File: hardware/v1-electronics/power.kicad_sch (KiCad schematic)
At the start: 35 parts, among them IC1 TPS61288LRQQR, IC2 MP2721GRH-0000-Z, J1 Female USB-C USB2.0, J2 Female JST-SH, SW7 SW_Push

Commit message: checkpoint(v1 hardware): this is the save before corrections
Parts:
- SW7: value SW_Push -> SW_SPDT; symbol Switch:SW_Push -> Switch:SW_SPDT
- renumbered D86 to D87
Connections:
- net V_IN_TPS: now also SW7.3 (C); no longer SW7.2
- net V_OUT_MP: now also SW7.2 (B); no longer SW7.1
- net VDD renamed V_REG0
- net V_OUT renamed +5V
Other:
- note added: "Consider adding a fuel gauge ic: - i2c and led indictor - BQ27220"
- note added: "is this the simplest power/usb-c module possible? Centralize the decoupling for +5V"
- note removed: "Consider Alternative Chargers: - BQ25883 [2 cell](i2c, power path, boost charger) - BQ25188 (i2c, power path) - BQ25619 Redo your power budget Consider adding a fuel gauge ic: - i2c and led indictor - BQ27220"
- note removed: "Figure out the battery situation and circuitry Conpare BQ25186DLHR and BQ25185DLHR"
- note removed: "Loose Notes"
- note removed: "is this the simplest power/usb-c module possible? Centralize the decoupling for V_SYS"
- moved on the sheet: C45, R56

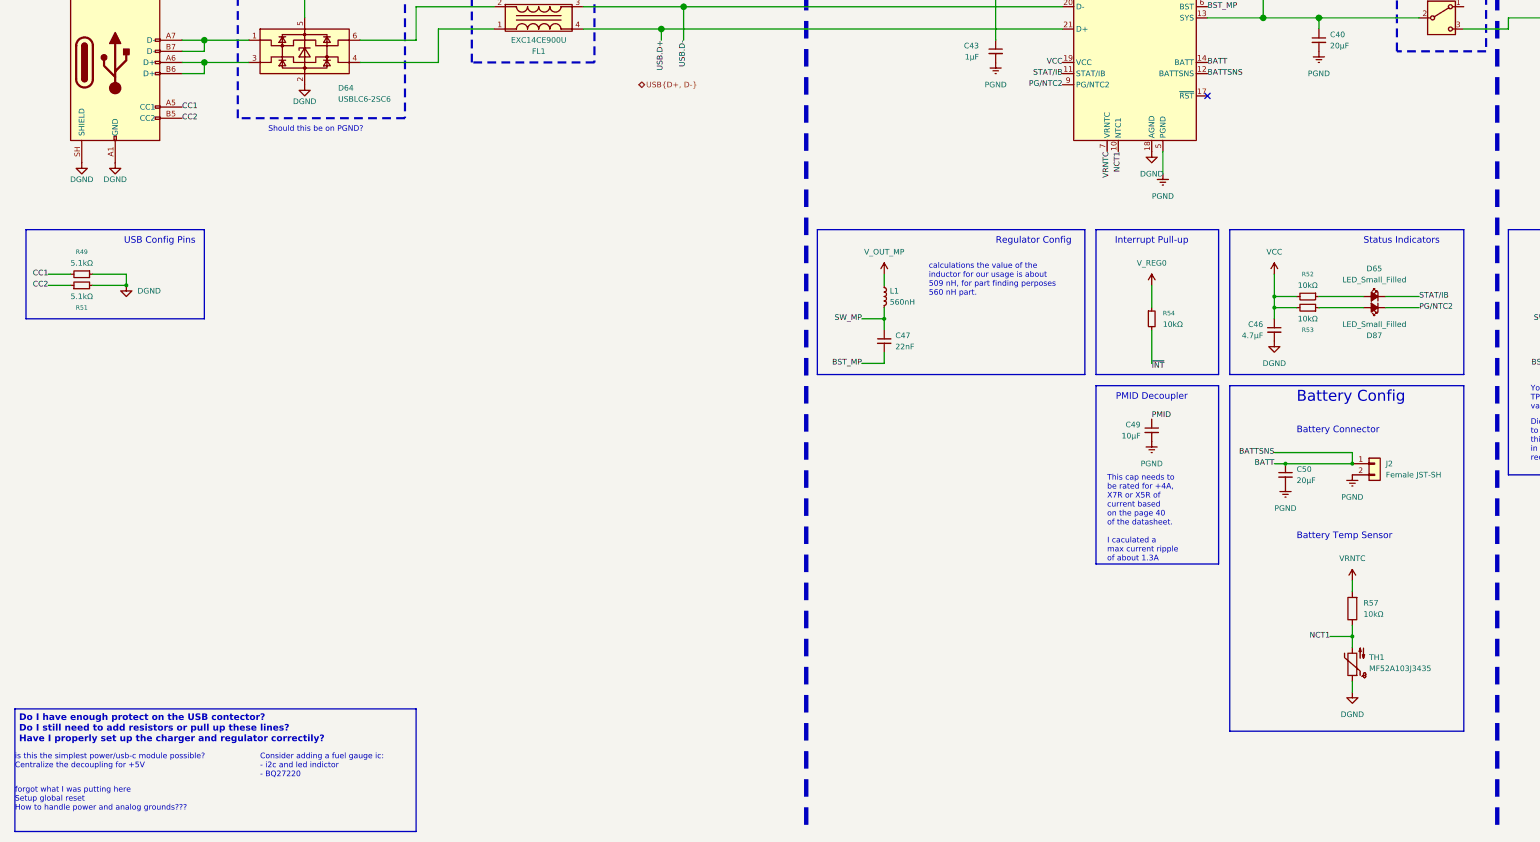
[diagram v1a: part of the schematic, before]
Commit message: fix(v1 hardware): implementing recommendations from Cyril
- rated the lines for the power system
- using a properly rated connecter for the battery
- added manual usb cc detection
- short grounds to each other
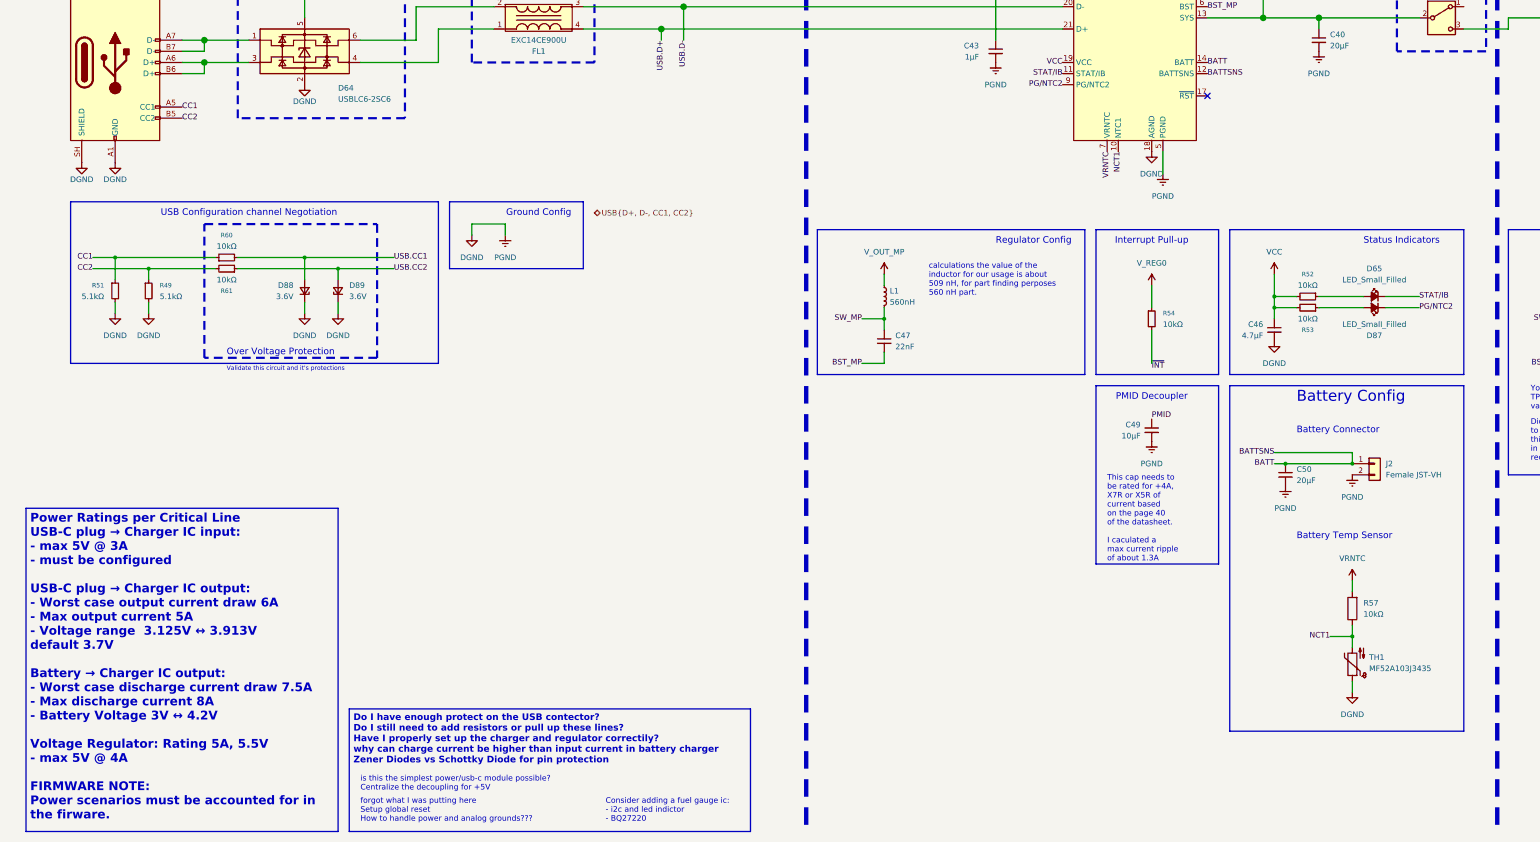
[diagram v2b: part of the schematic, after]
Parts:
- added D88, D89: 3.6V, symbol Device:D_Zener_Small
- added R60, R61: 10kΩ, symbol Device:R_Small
- J2: value Female JST-SH -> Female JST-VH
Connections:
- net PGND is gone; now on net DGND: C37.1, C38.1, C39.1, C40.2, C41.1, C42.1, C43.2, C49.2, C50.2, IC1.3 (PGND), IC2.5 (PGND), J2.2 (Pin_2)
- net CC1: now also R51.1, R60.1; no longer R49.2
- net CC2: now also R49.1, R61.2; no longer R51.1
- net DGND: now also R49.2, D88.1 (K), D89.1 (K); no longer R49.1
- new net USB.CC1: D88.2 (A), R60.2
- new net USB.CC2: D89.2 (A), R61.1
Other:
- note added: "Ground Config"
- note added: "Over Voltage Protection"
- note added: "USB Configuration channel Negotiation"
- note added: "Validate this circuit and it's protections"
- note removed: "Should this be on PGND?"
- note removed: "USB Config Pins"
- moved on the sheet: R49, R51

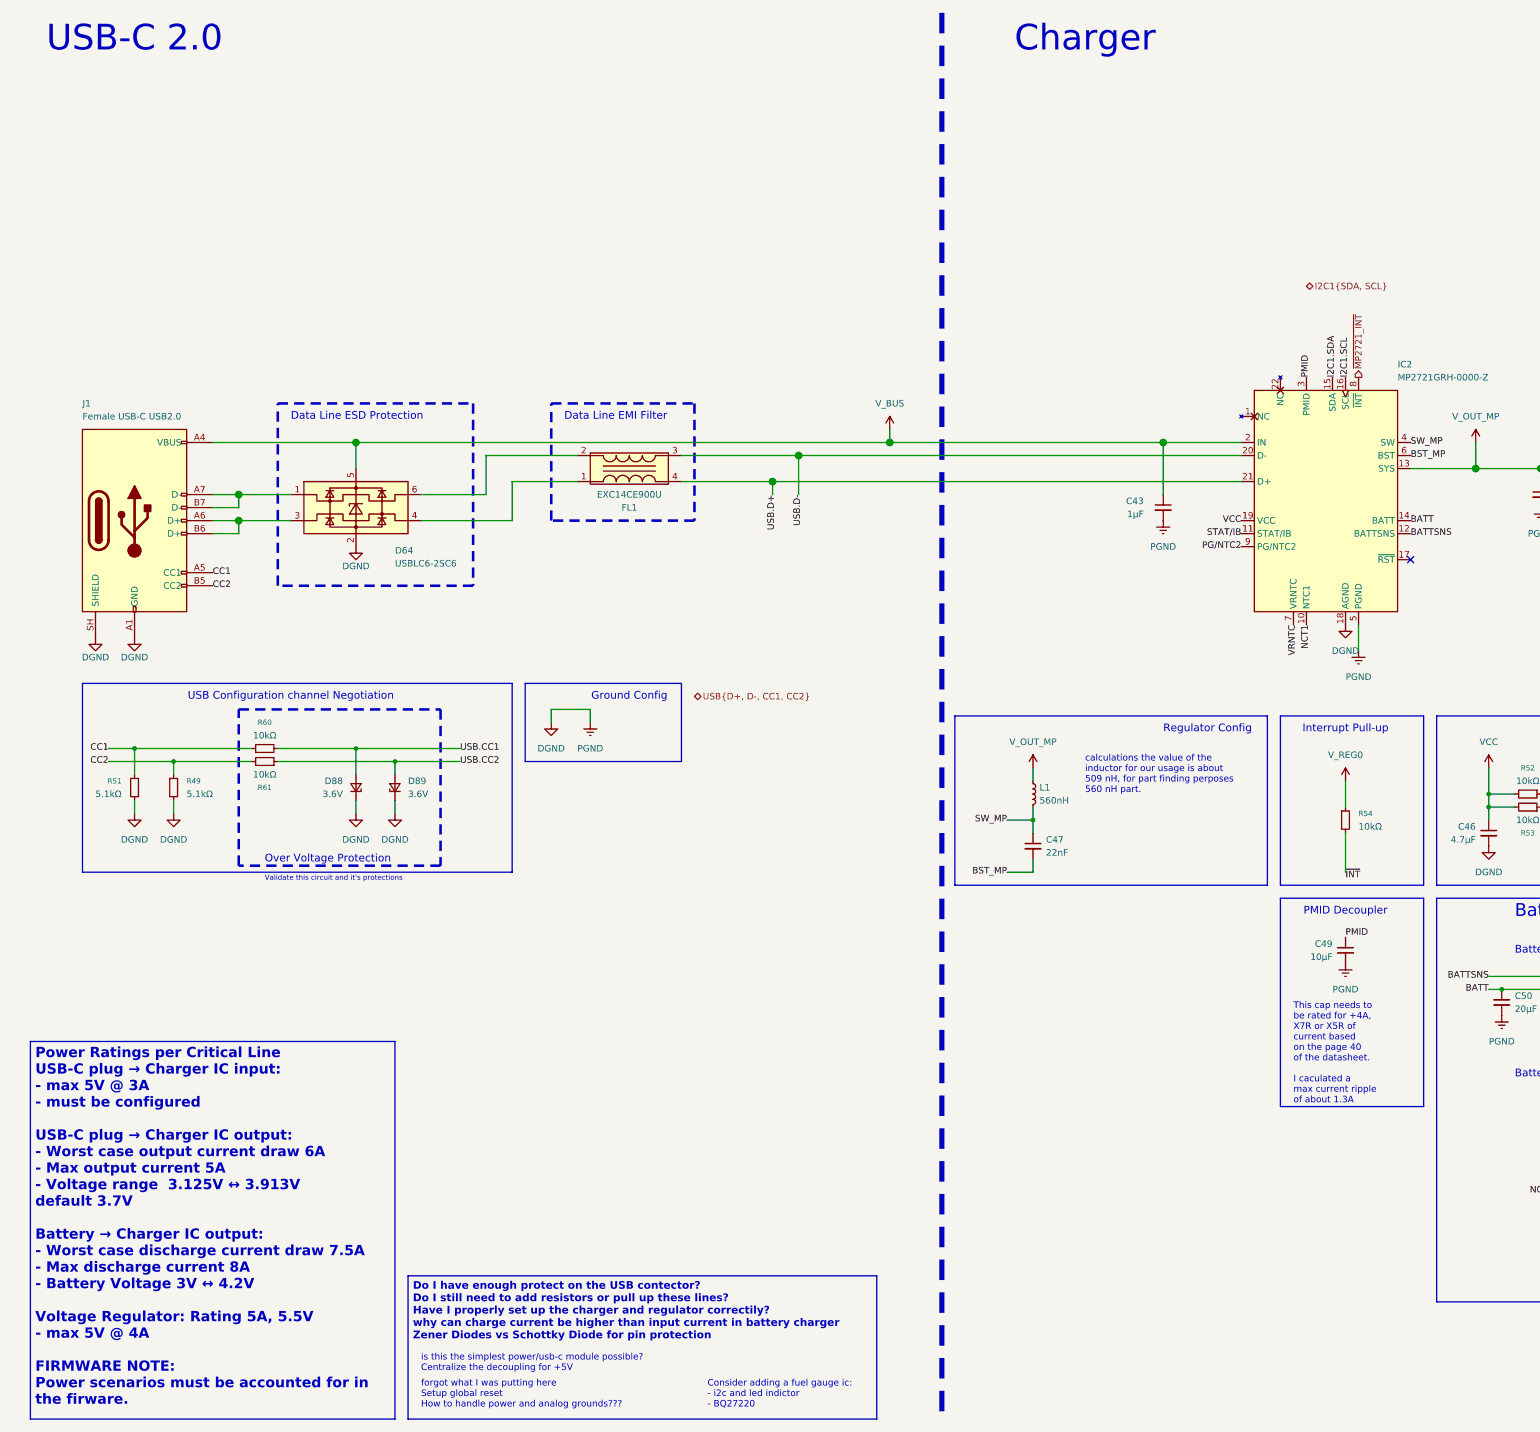
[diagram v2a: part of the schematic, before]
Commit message: fix(v1 hardware): complete set of recommendations
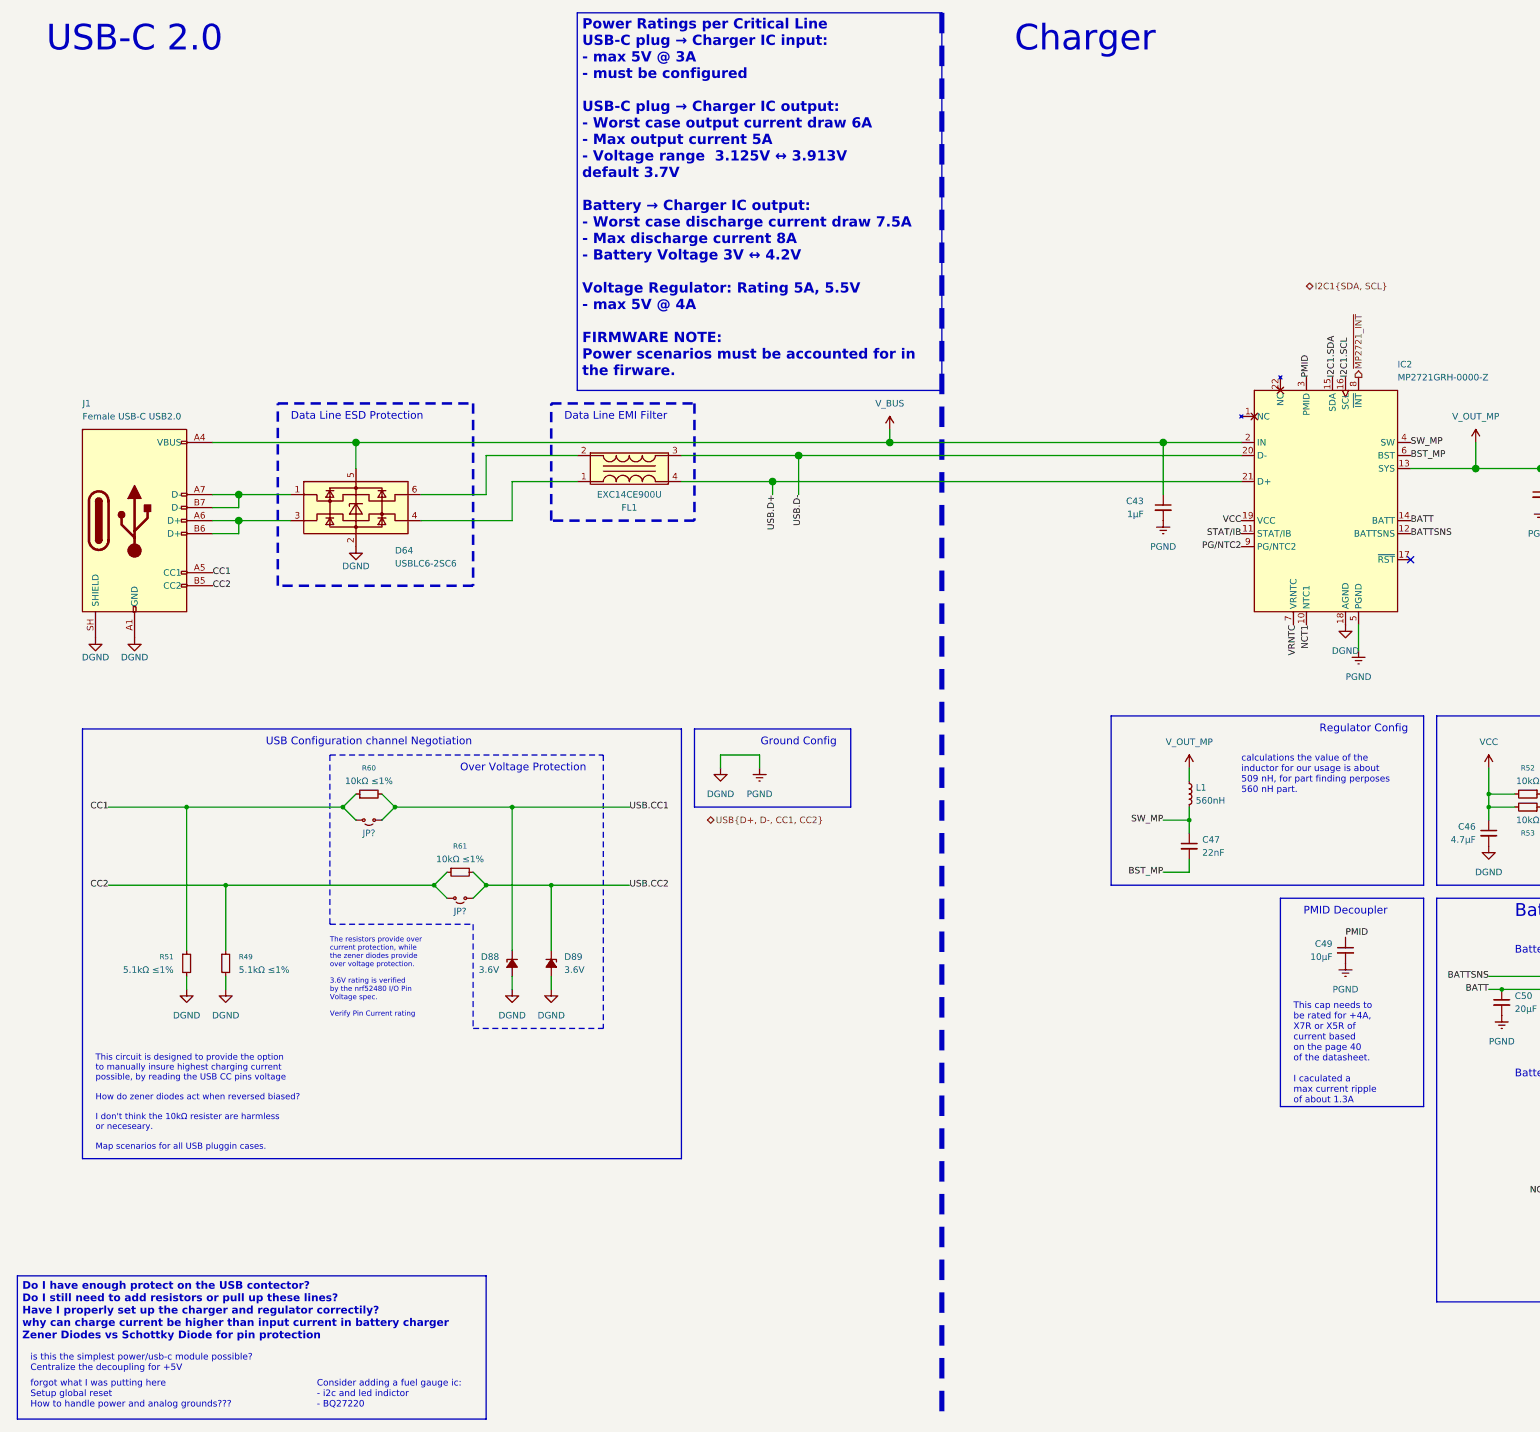
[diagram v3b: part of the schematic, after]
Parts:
- removed D88, D89: 3.6V, symbol Device:D_Zener_Small
- removed R54: 10kΩ, symbol Device:R_Small
- added D88, D89: 3.6V, symbol Device:D_Zener_Small_Filled
- added JP? (x2): Jumper_2_Small_Open, symbol Jumper:Jumper_2_Small_Open
- R49, R51: value 5.1kΩ -> 5.1kΩ ≤1%
- R60, R61: value 10kΩ -> 10kΩ ≤1%
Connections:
- net CC1: now also JP?.1 (A)
- net CC2: now also R61.1, JP?.1 (A); no longer R61.2
- net DGND: now also D88.2 (A), D89.2 (A)
- net USB.CC1: now also D88.1 (K), JP?.2 (B)
- net USB.CC2: now also R61.2, D89.1 (K), JP?.2 (B); no longer R61.1
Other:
- note added: "The resistors provide over current protection, while the zener diodes provide over voltage protection. 3.6V rating is verified by the nrf52480 I/O Pin Voltage spec. Verify Pin Current rating"
- note added: "This circuit is designed to provide the option to manually insure highest charging current possible, by reading the USB CC pins voltage How do zener diodes act when reversed biased? I don't think the 10kΩ resister are harmless or neceseary. Map scenarios for all USB pluggin cases."
- note removed: "Interrupt Pull-up"
- note removed: "Validate this circuit and it's protections"
- moved on the sheet: C47, L1, R49, R51, R60, R61
